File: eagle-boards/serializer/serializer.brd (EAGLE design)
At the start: 64.9 x 80.5 mm, 8 parts, among them IC1 74LS93N, IC2 74LS151N, IC3 74LS86N, IC4 74LS04N

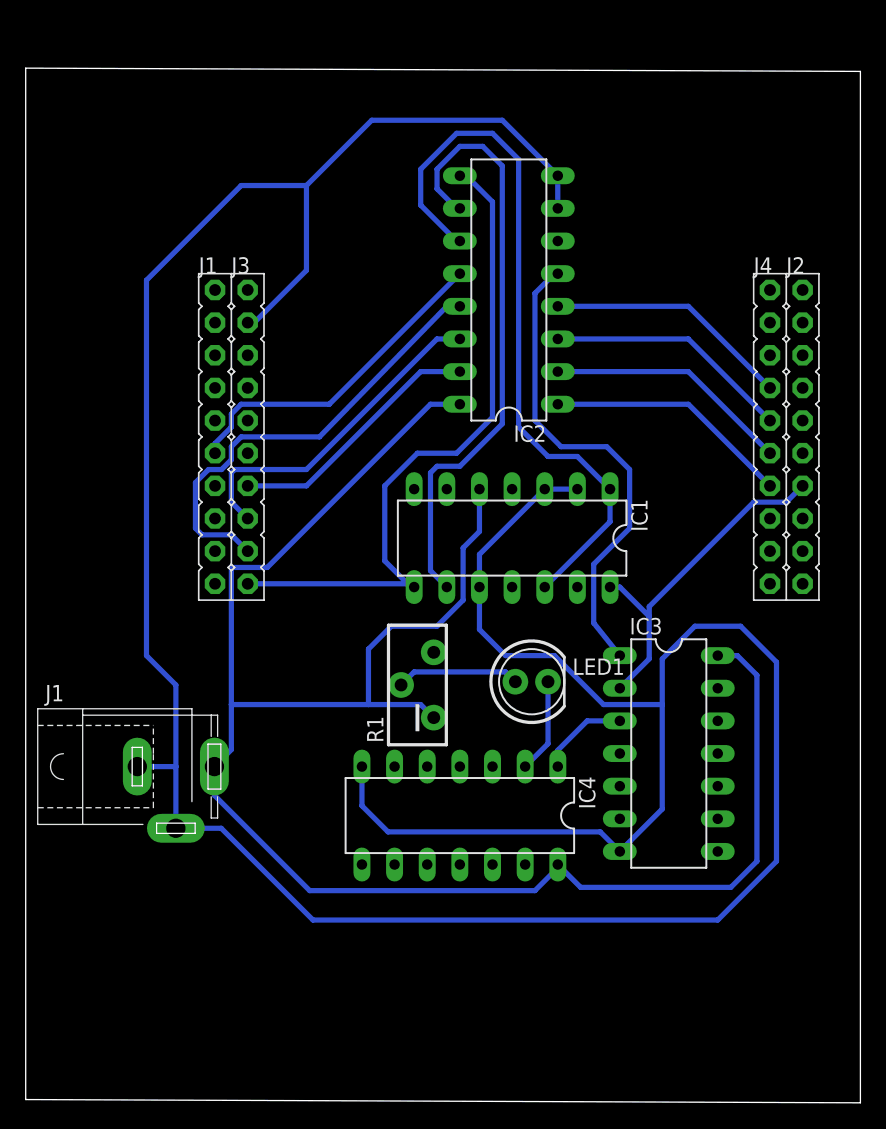
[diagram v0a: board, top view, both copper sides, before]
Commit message: Transmit code working with PLL
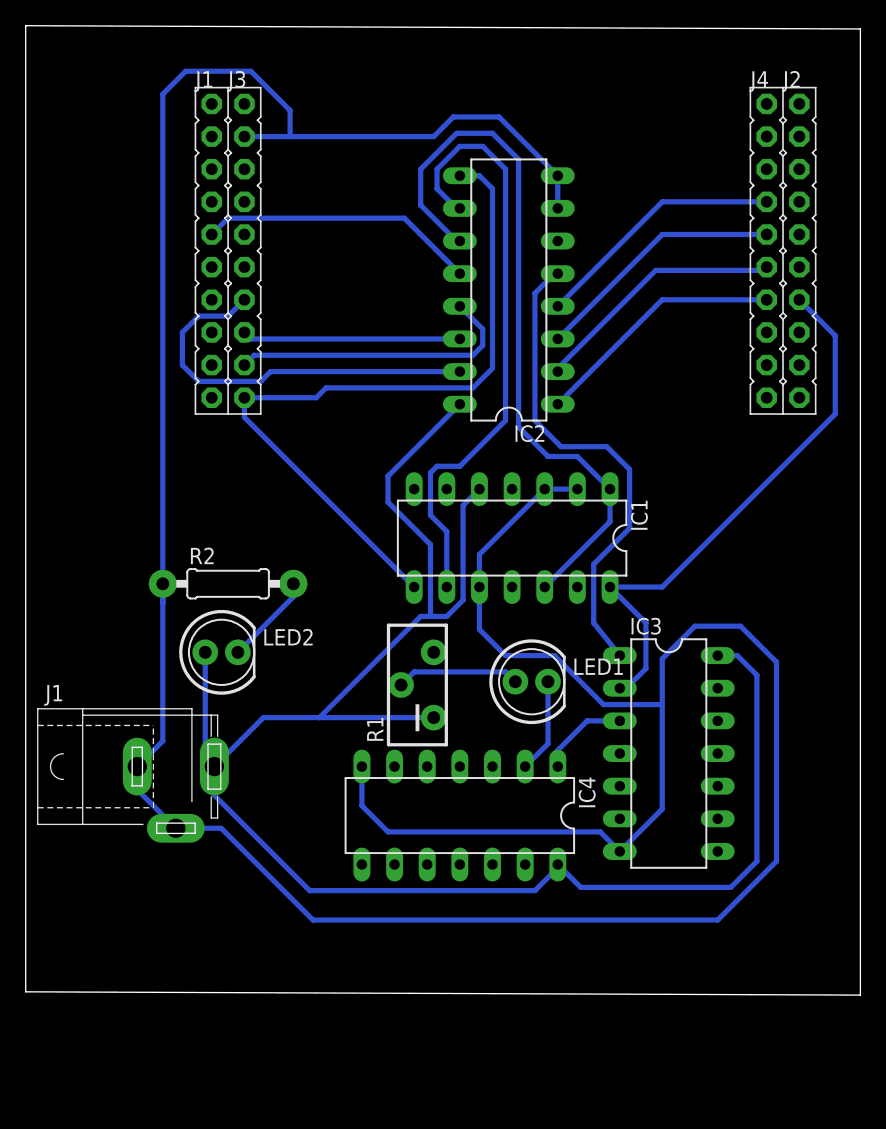
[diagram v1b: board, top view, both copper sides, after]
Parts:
- added LED2: (no value), led:LED5MM
- added R2: (no value), rcl:0207/10
- moved U$1 14.5 mm to (30.7, 69.8)
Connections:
- new net N$2: LED2.K, R2.2
- net +5: now also LED2.A
- net D7: now also U$1.PE4; no longer U$1.PE5
- net GND: now also R2.1
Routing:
- net CLK: track 27.1 -> 43.3 mm
- net D6: track 35.3 -> 23.0 mm
- net D4: track 20.2 -> 30.8 mm
- net D5: track 26.2 -> 17.0 mm
- net N$2: track 0.00 -> 7.12 mm
- net +5: track 145.9 -> 140.4 mm
- net CLK/16: track 52.2 -> 57.4 mm
- net D7: track 25.9 -> 21.6 mm
- net GND: track 252.3 -> 255.4 mm
- net D2: track 19.1 -> 19.8 mm
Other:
- board size 64.9 x 80.5 mm -> 64.9 x 75.4 mm
